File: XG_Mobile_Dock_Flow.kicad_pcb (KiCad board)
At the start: 4 copper layers, 220 x 65 mm, 81 parts, among them J1 5-1775443-8, J10 SWD, J11 UART, J12 I2C1, J13 39300240, J14 469911008, J17 8730, J2 20455-040E-76, J3 20455-040E-76, J4 3-2362375-4, J5 USB_C_Receptacle, Q16 AO3401A, Q17 2N7002W, SW1 SW_Push, U1 DS160PR410RNQR, U12 STM32F030C8Tx, U2 DS160PR410RNQR

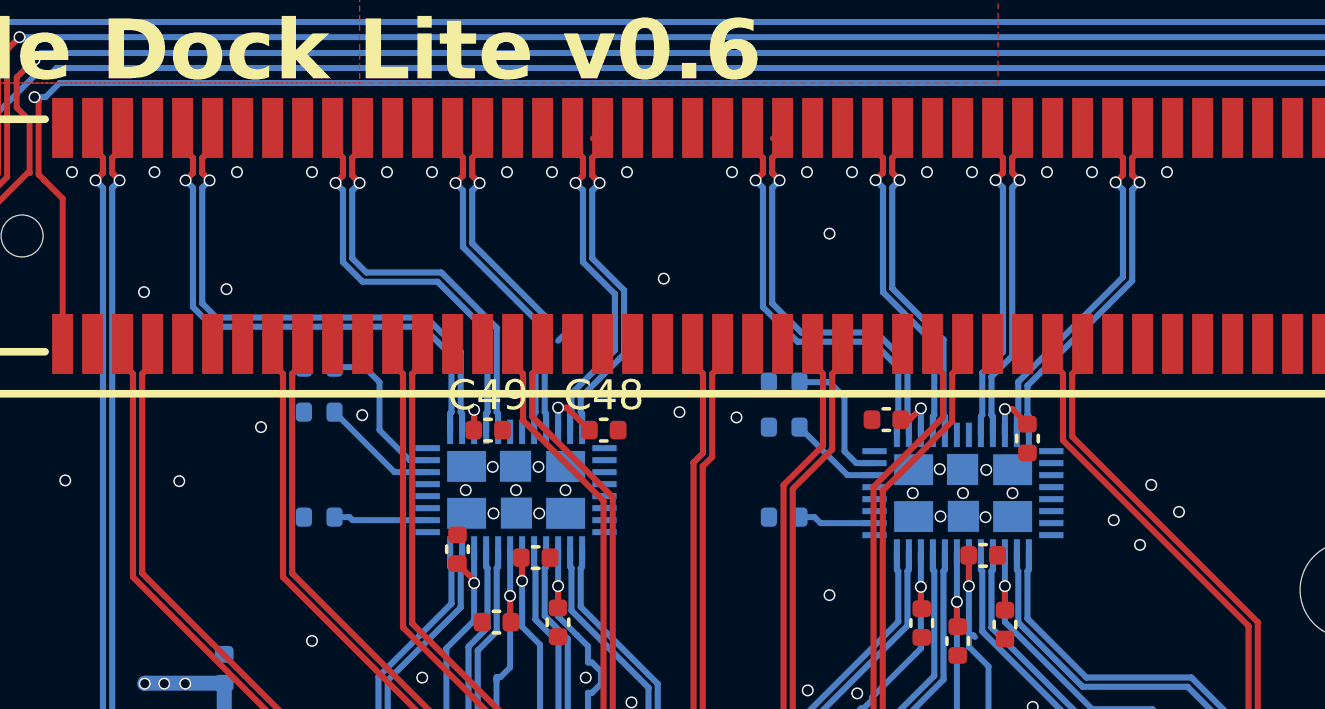
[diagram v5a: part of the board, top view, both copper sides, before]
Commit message: added missing ac decoupler caps
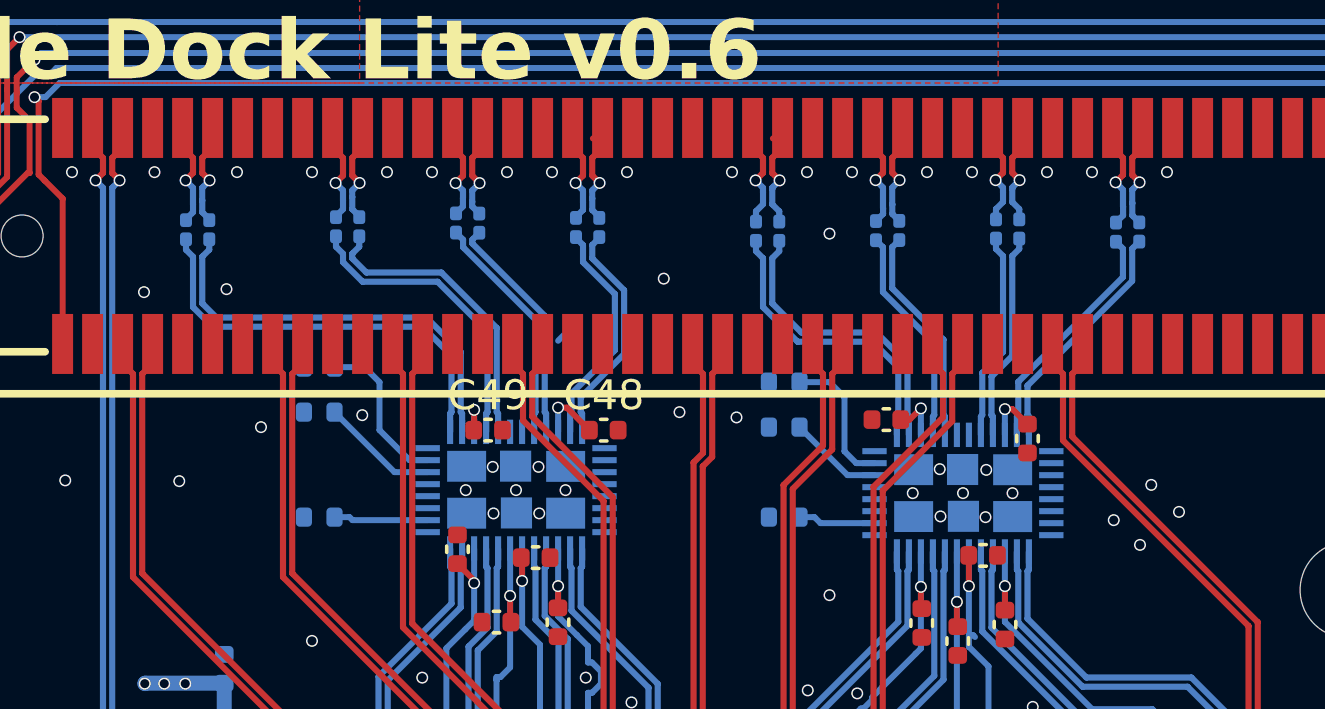
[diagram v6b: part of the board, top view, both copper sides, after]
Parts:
- added C1: 220nF, Capacitor_SMD:C_0201_0603Metric, B.Cu at (95.0, 59.9)
- added C10: 220nF, Capacitor_SMD:C_0201_0603Metric, B.Cu at (118.8, 59.9)
- added C11: 220nF, Capacitor_SMD:C_0201_0603Metric, B.Cu at (122.0, 59.9)
- added C12: 220nF, Capacitor_SMD:C_0201_0603Metric, B.Cu at (122.8, 59.9)
- added C13: 220nF, Capacitor_SMD:C_0201_0603Metric, B.Cu at (126.0, 60.0)
- added C14: 220nF, Capacitor_SMD:C_0201_0603Metric, B.Cu at (126.8, 60.0)
- added C15: 220nF, Capacitor_SMD:C_0201_0603Metric, B.Cu at (100.0, 59.8)
- added C16: 220nF, Capacitor_SMD:C_0201_0603Metric, B.Cu at (100.8, 59.8)
- added C2: 220nF, Capacitor_SMD:C_0201_0603Metric, B.Cu at (95.8, 59.9)
- added C3: 220nF, Capacitor_SMD:C_0201_0603Metric, B.Cu at (104.0, 59.7)
- added C4: 220nF, Capacitor_SMD:C_0201_0603Metric, B.Cu at (104.8, 59.7)
- added C5: 220nF, Capacitor_SMD:C_0201_0603Metric, B.Cu at (108.0, 59.8)
- added C6: 220nF, Capacitor_SMD:C_0201_0603Metric, B.Cu at (108.8, 59.8)
- added C7: 220nF, Capacitor_SMD:C_0201_0603Metric, B.Cu at (114.0, 60.0)
- added C8: 220nF, Capacitor_SMD:C_0201_0603Metric, B.Cu at (114.8, 60.0)
- added C9: 220nF, Capacitor_SMD:C_0201_0603Metric, B.Cu at (118.0, 60.0)
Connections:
- U1 pad 10: /HSI4N -> /HSIT4N
- U1 pad 12: /HSI5P -> /HSIT5P
- U1 pad 13: /HSI5N -> /HSIT5N
- U1 pad 16: /HSI6P -> /HSIT6P
- U1 pad 17: /HSI6N -> /HSIT6N
- U1 pad 19: /HSI7P -> /HSIT7P
- U1 pad 20: /HSI7N -> /HSIT7N
- U1 pad 9: /HSI4P -> /HSIT4P
- U2 pad 10: /HSI0N -> /HSIT0N
- U2 pad 12: /HSI1P -> /HSIT1P
- U2 pad 13: /HSI1N -> /HSIT1N
- U2 pad 16: /HSI2P -> /HSIT2P
- U2 pad 17: /HSI2N -> /HSIT2N
- U2 pad 19: /HSI3P -> /HSIT3P
- U2 pad 20: /HSI3N -> /HSIT3N
- U2 pad 9: /HSI0P -> /HSIT0P
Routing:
- net /HSI0P: track 18.2 -> 3.52 mm
- net /HSI0N: track 18.2 -> 3.52 mm
- net /HSIT0N: track 0.00 -> 14.2 mm
- net /HSIT0P: track 0.00 -> 14.2 mm
- net /HSI1N: track 14.0 -> 3.42 mm
- net /HSI1P: track 14.0 -> 3.42 mm
- net /HSI4N: track 14.2 -> 3.87 mm
- net /HSI4P: track 13.9 -> 3.57 mm
- net /HSIT1P: track 0.00 -> 10.1 mm
- net /HSIT1N: track 0.00 -> 10.1 mm
- net /HSIT4P: track 0.00 -> 9.92 mm
- net /HSIT4N: track 0.00 -> 9.92 mm
- net /HSI7N: track 12.2 -> 3.73 mm
- net /HSI7P: track 12.0 -> 3.60 mm
- net /HSI2P: track 11.5 -> 3.29 mm
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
